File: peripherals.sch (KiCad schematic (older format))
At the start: 23 parts, among them J3 CTC Header, J5 Port B, J6 Port A, J7 PIO Header, U4 CTC - Z84C3010AEG, U5 SIO/3 - Z84C4310AEG, U7 Z84C2010AEG

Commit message: reset annotations, added dip switch
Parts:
- renumbered J3 to J6, J5 to J7, J6 to J8, J7 to J9, R27 to R36, R28 to R37, R29 to R38, R30 to R39, R31 to R40, R32 to R41, R33 to R42, R34 to R43, R35 to R44, R36 to R45, R37 to R46, R38 to R47, R39 to R48, R40 to R49, R41 to R50, R42 to R51, U4 to U7, U5 to U8, U7 to U9

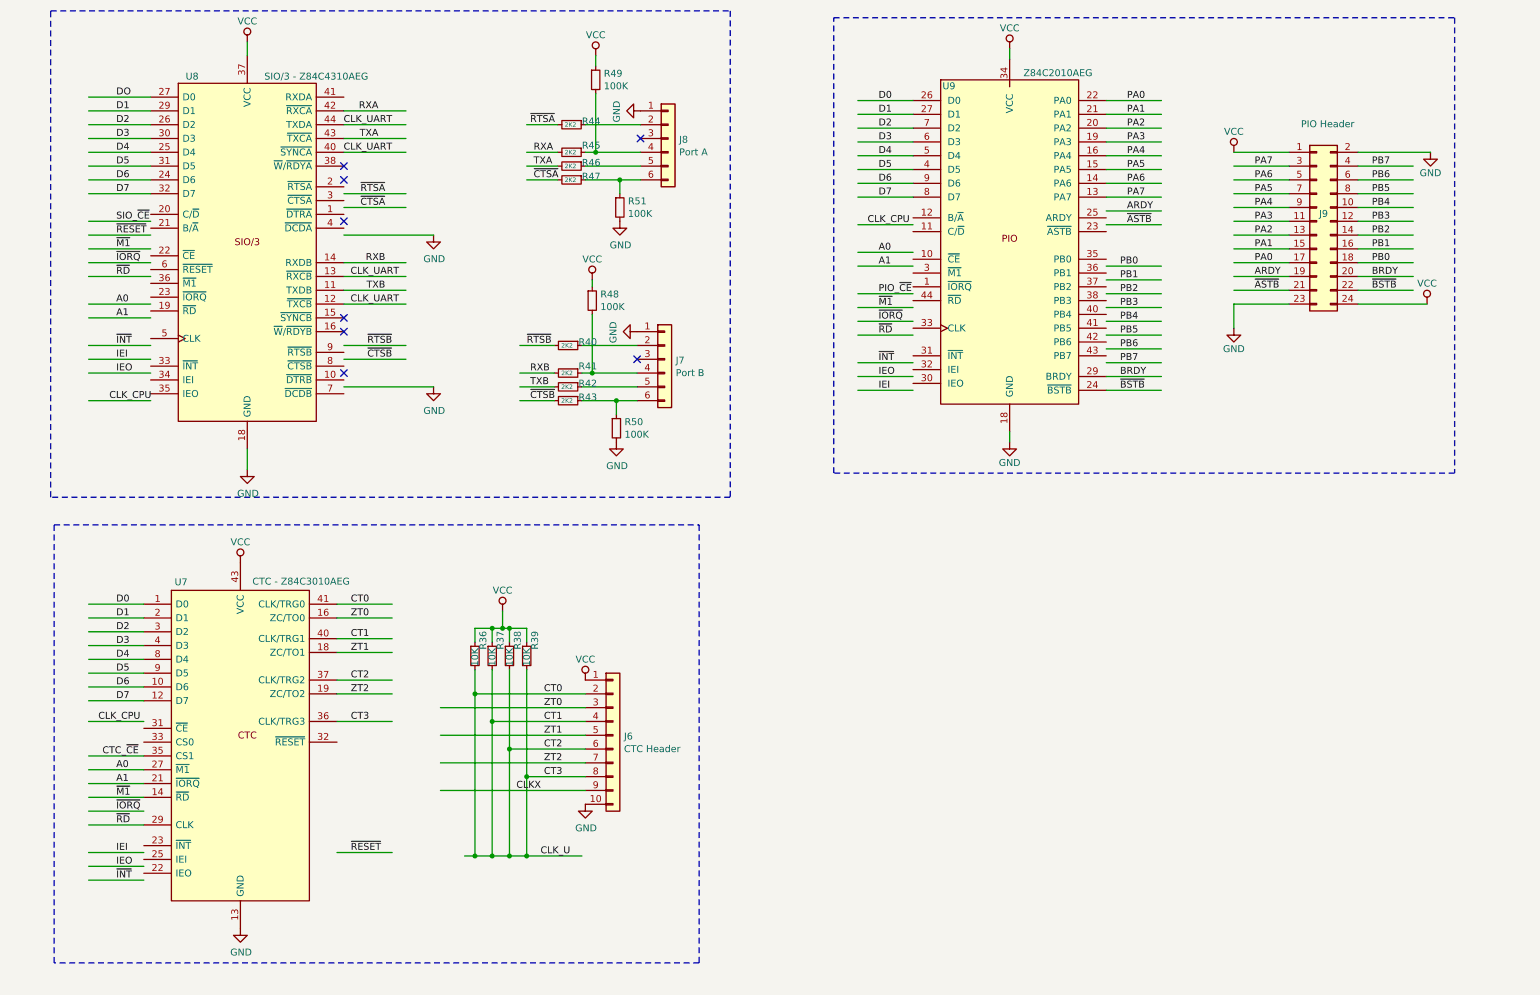
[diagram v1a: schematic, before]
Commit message: connect sheet pins
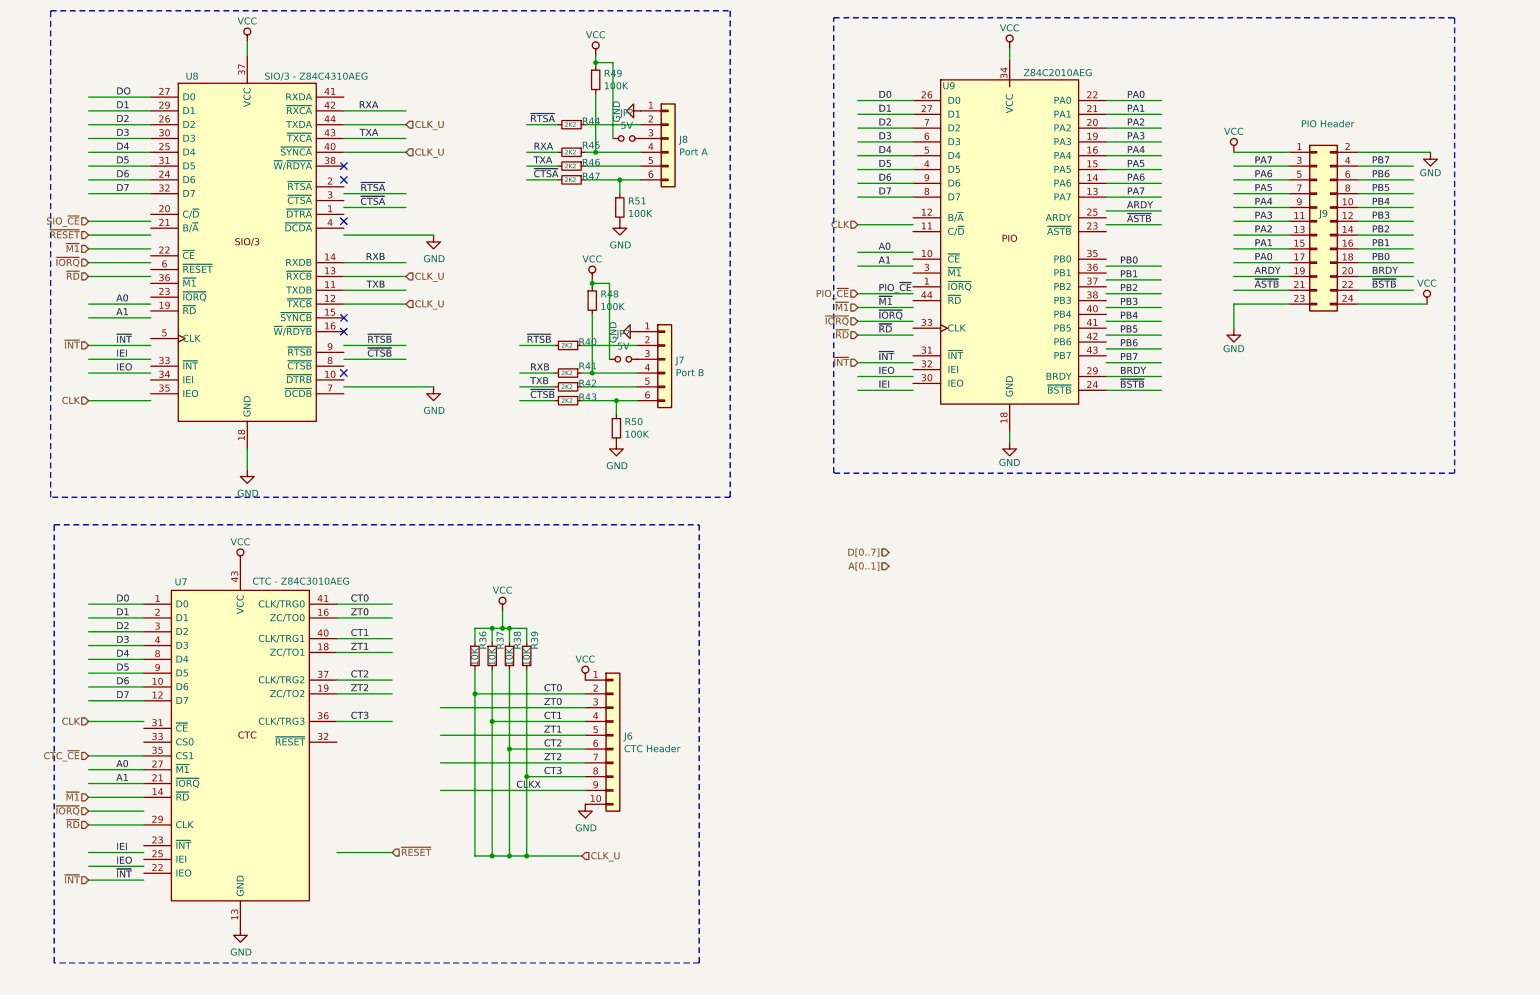
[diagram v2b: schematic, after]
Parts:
- added JP? (x2): 5V, Connector_PinHeader_2.54mm:PinHeader_1x02_P2.54mm_Vertical, symbol Device:Jumper_NO_Small
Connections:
- net labels added: A[0..1], CLK, CTC_~CE, D[0..7], PIO_~CE, SIO_~CE
- net labels removed: CLK_CPU, CLK_UART, CTC_~CE~, SIO_~CE~
- wire segments 182 -> 187
- no-connect marks 8 -> 6
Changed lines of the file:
@@
 $Descr A4 11693 8268
 encoding utf-8
-Sheet 3 3
+Sheet 2 3
 Title ""
 Date ""
@@
 Text Label 6625 1950 0    50   ~ 0
 D7
-Text Label 6850 2150 2    50   ~ 0
-CLK_CPU
 Text Label 6625 2350 0    50   ~ 0
 A0
@@
 Text Label 4100 3225 0    50   ~ 0
 RXB
-Text Label 3150 2725 2    50   ~ 0
-CLK_UART
-Text Label 3150 2525 2    50   ~ 0
-CLK_UART
-Text Label 1100 2125 0    50   ~ 0
-SIO_~CE~
-Text Label 3100 1625 2    50   ~ 0
-CLK_UART
-Text Label 3100 1425 2    50   ~ 0
-CLK_UART
 Text Label 3100 3025 2    50   ~ 0
 ~RTSB
@@
 	1    0    0    -1
 $EndComp
-Text Label 1050 3425 0    50   ~ 0
-CLK_CPU
 Text Label 1100 3225 0    50   ~ 0
 IEO
@@
 Text Label 1100 2725 0    50   ~ 0
 A0
-Text Label 1100 2525 0    50   ~ 0
-~RD
-Text Label 1100 2325 0    50   ~ 0
-~M1
 $Comp
 L THS-80:Z84C4310AEG U?
@@
 	1    0    0    -1
 $EndComp
-Text Label 1100 2225 0    50   ~ 0
-~RESET
-Text Label 1100 2425 0    50   ~ 0
-~IORQ
-Wire Wire Line
-	4575 925  4575 1000
-Wire Wire Line
-	4550 2550 4550 2600
+Wire Wire Line
+	4575 925  4575 975
+Wire Wire Line
+	4550 2550 4550 2575
 Wire Wire Line
 	4275 3425 4025 3425
@@
 Wire Wire Line
 	4900 1425 4500 1425
-NoConn ~ 4900 1525
 Connection ~ 4725 3425
 Connection ~ 4550 3225
-NoConn ~ 4875 3125
 Connection ~ 4750 1825
 Connection ~ 4575 1625
@@
 Wire Wire Line
 	1300 6900 900  6900
-Text Label 1275 5750 2    50   ~ 0
-CLK_CPU
-Text Label 1000 6000 0    50   ~ 0
-CTC_~CE~
 Text Label 1100 6800 0    50   ~ 0
 IEO
@@
 Text Label 1100 6700 0    50   ~ 0
 IEI
-Text Label 1100 6300 0    50   ~ 0
-~M1
-Text Label 1100 6400 0    50   ~ 0
-~IORQ
-Text Label 1100 6500 0    50   ~ 0
-~RD
 Text Label 1100 6100 0    50   ~ 0
 A0
@@
 Text Label 2800 5750 0    50   ~ 0
 CT3
-Text Label 2800 6700 0    50   ~ 0
-~RESET
 Wire Wire Line
 	3450 5650 4500 5650
@@
 Wire Wire Line
 	3450 6250 4500 6250
-Wire Wire Line
-	3625 6725 3700 6725
 Wire Wire Line
 	4075 6150 4075 6725
@@
 	3700 5550 3700 6725
 Connection ~ 3700 5550
-Connection ~ 3700 6725
 Wire Wire Line
 	3700 6725 3825 6725
-Text Label 4175 6725 0    50   ~ 0
-CLK_U
 Wire Notes Line
 	650  4325 5325 4325
@@
 Wire Wire Line
 	9200 2725 9200 2900
+Text HLabel 6700 4525 0    50   Input ~ 0
+D[0..7]
+Text HLabel 6700 4625 0    50   Input ~ 0
+A[0..1]
+Text HLabel 3100 6700 2    50   Input ~ 0
+~RESET
+Text HLabel 900  5750 0    50   Input ~ 0
+CLK
+Text HLabel 900  6000 0    50   Input ~ 0
+CTC_~CE
+Text HLabel 900  6300 0    50   Input ~ 0
+~M1
+Text HLabel 900  6400 0    50   Input ~ 0
+~IORQ
+Text HLabel 900  6500 0    50   Input ~ 0
+~RD
+Text HLabel 900  2225 0    50   Input ~ 0
+~RESET
+Text HLabel 900  2125 0    50   Input ~ 0
+SIO_~CE
+Text HLabel 900  2325 0    50   Input ~ 0
+~M1
+Text HLabel 900  2425 0    50   Input ~ 0
+~IORQ
+Text HLabel 900  2525 0    50   Input ~ 0
+~RD
+Text HLabel 900  3425 0    50   Input ~ 0
+CLK
+Text HLabel 6475 2150 0    50   Input ~ 0
+CLK
+Text HLabel 6475 2750 0    50   Input ~ 0
+~M1
+Text HLabel 6475 2850 0    50   Input ~ 0
+~IORQ
+Text HLabel 6475 2950 0    50   Input ~ 0
+~RD
+Text HLabel 6475 2650 0    50   Input ~ 0
+PIO_~CE
+Text HLabel 900  3025 0    50   Input ~ 0
+~INT
+Text HLabel 900  6900 0    50   Input ~ 0
+~INT
+Text HLabel 6475 3150 0    50   Input ~ 0
+~INT
+Text HLabel 4475 6725 2    50   Input ~ 0
+CLK_U
+$Comp
+L Device:Jumper_NO_Small JP?
+U 1 1 5D92266C
+P 4775 3125
+F 0 "JP?" H 4775 3310 50  0000 C CNN
+F 1 "5V" H 4775 3219 50  0000 C CNN
+F 2 "Connector_PinHeader_2.54mm:PinHeader_1x02_P2.54mm_Vertical" H 4775 3125 50  0001 C CNN
+F 3 "~" H 4775 3125 50  0001 C CNN
+	1    4775 3125
+	1    0    0    -1
+$EndComp
+Wire Wire Line
+	4675 3125 4675 2575
+Wire Wire Line
+	4675 2575 4550 2575
+Connection ~ 4550 2575
+Wire Wire Line
+	4550 2575 4550 2600
+$Comp
+L Device:Jumper_NO_Small JP?
+U 1 1 5D934FDF
+P 4800 1525
+F 0 "JP?" H 4800 1710 50  0000 C CNN
+F 1 "5V" H 4800 1619 50  0000 C CNN
+F 2 "Connector_PinHeader_2.54mm:PinHeader_1x02_P2.54mm_Vertical" H 4800 1525 50  0001 C CNN
+F 3 "~" H 4800 1525 50  0001 C CNN
+	1    4800 1525
+	1    0    0    -1
+$EndComp
+Wire Wire Line
+	4700 1525 4700 975
+Wire Wire Line
+	4700 975  4575 975
+Connection ~ 4575 975
+Wire Wire Line
+	4575 975  4575 1000
+Text HLabel 3200 2725 2    50   Input ~ 0
+CLK_U
+Text HLabel 3200 2525 2    50   Input ~ 0
+CLK_U
+Text HLabel 3200 1625 2    50   Input ~ 0
+CLK_U
+Text HLabel 3200 1425 2    50   Input ~ 0
+CLK_U
 $EndSCHEMATC

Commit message: connected sheet pins to bus
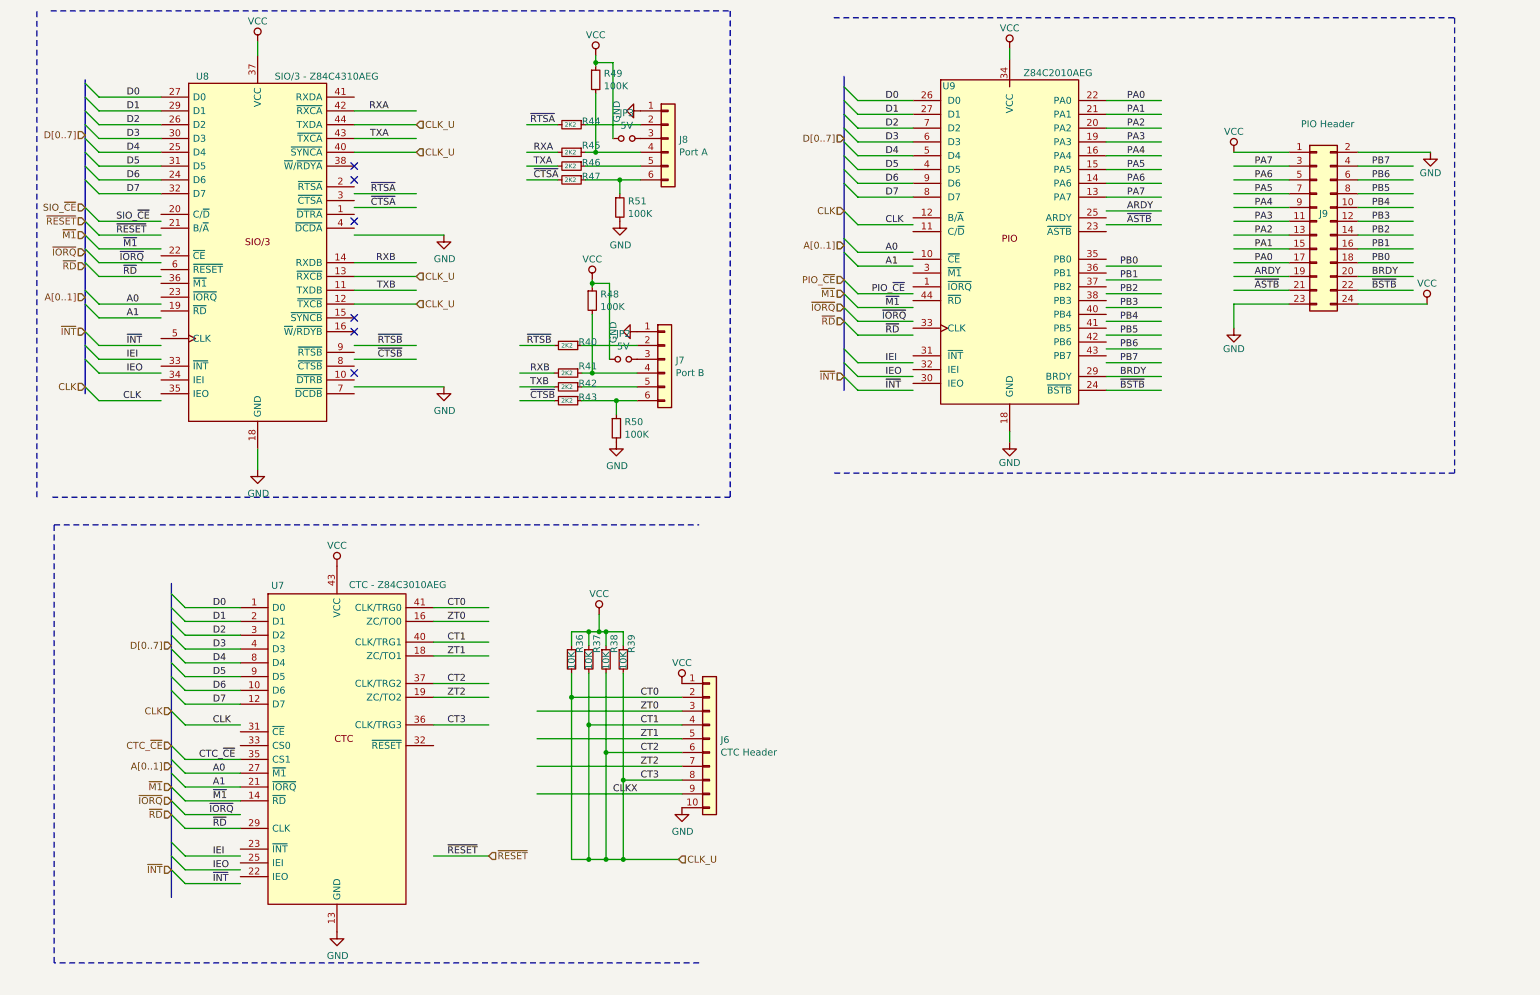
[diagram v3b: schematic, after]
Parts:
- gave numbers to parts that had none: 2
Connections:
- net labels removed: DO, PIO_~CE~
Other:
- moved on the sheet: J6, R36, R37, R38, R39, U7, U8

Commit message: Moved CPU, RAM, ROM to sub-sheet
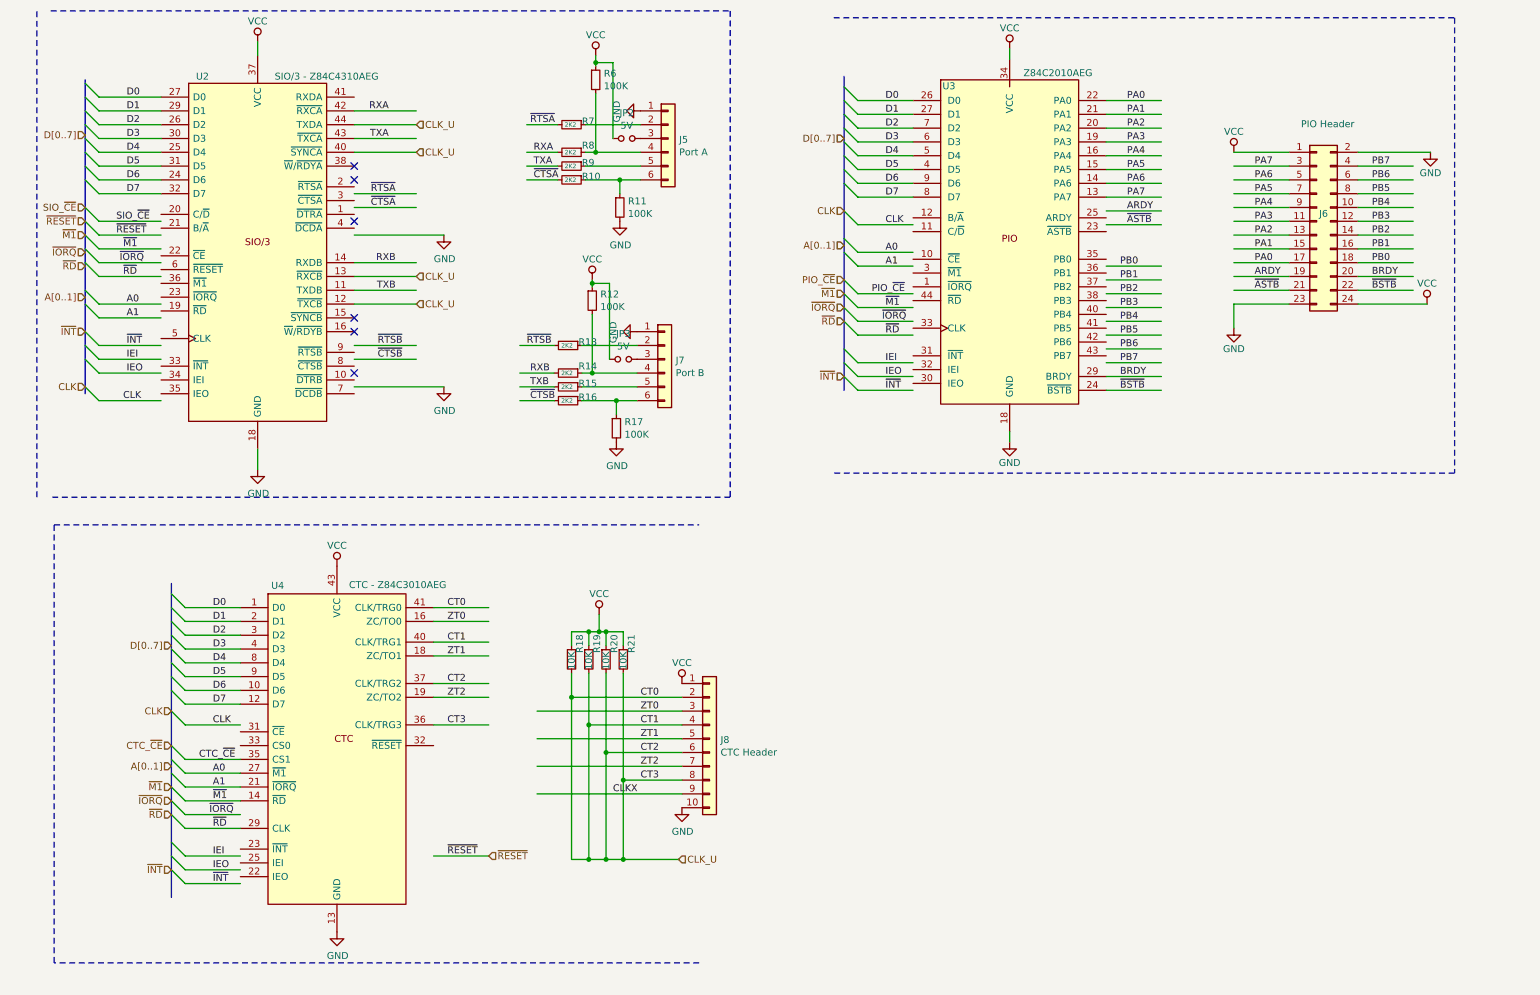
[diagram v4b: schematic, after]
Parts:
- renumbered J8 to J5, J9 to J6, J6 to J8, JP3 to JP2, JP2 to JP3, R47 to R10, R51 to R11, R48 to R12, R40 to R13, R41 to R14, R42 to R15, R43 to R16, R50 to R17, R36 to R18, R37 to R19, R38 to R20, R39 to R21, R49 to R6, R44 to R7, R45 to R8, R46 to R9, U8 to U2, U9 to U3, U7 to U4

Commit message: fixed up interrupt chain wiring
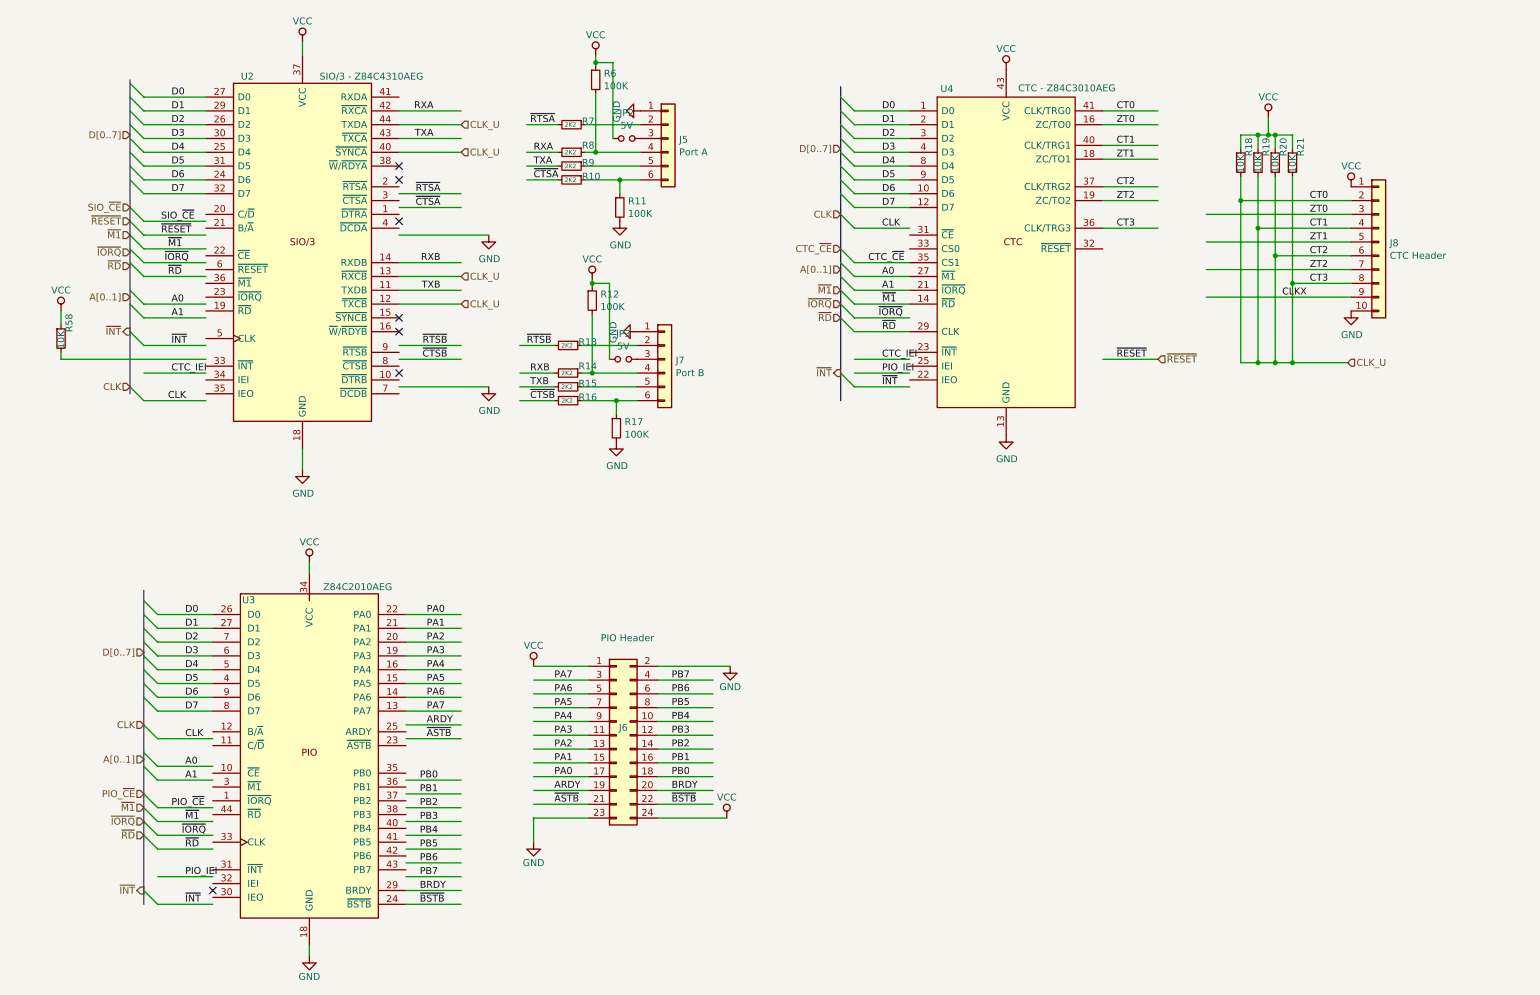
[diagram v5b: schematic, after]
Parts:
- added R58: 10K, Resistor_SMD:R_0603_1608Metric_Pad1.05x0.95mm_HandSolder, symbol THS-80-rescue:R_Small-Device-sbc_z80-rescue
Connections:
- net labels added: CTC_IEI, PIO_IEI
- net labels removed: IEI, IEO
- wire segments 187 -> 188
- no-connect marks 6 -> 7
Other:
- moved on the sheet: J6, J8, R18, R19, R20, R21, U2, U3, U4

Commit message: passed DRC
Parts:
- removed R58: 10K, Resistor_SMD:R_0603_1608Metric_Pad1.05x0.95mm_HandSolder, symbol THS-80-rescue:R_Small-Device-sbc_z80-rescue
- removed U2: SIO/3 - Z84C4310AEG, Package_QFP:LQFP-44_10x10mm_P0.8mm, symbol THS-80:Z84C4310AEG
- removed U3: Z84C2010AEG, Package_QFP:LQFP-44_10x10mm_P0.8mm, symbol THS-80:Z84C2010AEG
- removed U4: CTC - Z84C3010AEG, Package_QFP:LQFP-44_10x10mm_P0.8mm, symbol THS-80:Z84C3010AEG
- added C19, C20, C21: 100nF, Capacitor_SMD:C_0603_1608Metric_Pad1.05x0.95mm_HandSolder, symbol Device:C_Small
- added R22: 10K, Resistor_SMD:R_0603_1608Metric_Pad1.05x0.95mm_HandSolder, symbol Device:R_Small
- added U7: Z84C2010AEG, Package_QFP:LQFP-44_10x10mm_P0.8mm, symbol THS-80:Z84C2010AEG
- added U8: Z84C4310AEG, Package_QFP:LQFP-44_10x10mm_P0.8mm, symbol THS-80:Z84C4310AEG
- added U9: Z84C3010AEG, Package_QFP:LQFP-44_10x10mm_P0.8mm, symbol THS-80:Z84C3010AEG
- renumbered J8 to J10, J6 to J7, J7 to J8, J5 to J9, JP3 to JP2, JP2 to JP3, R13 to R23, R14 to R24, R15 to R25, R16 to R26, R7 to R27, R8 to R28, R9 to R29, R10 to R30, R12 to R31, R6 to R32, R17 to R33, R11 to R34, R18 to R35, R19 to R36, R20 to R37, R21 to R38
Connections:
- net labels added: CLK_A, CLK_B, CLK_C, IEI, IEO, IEO_0, IEO_1, PIO_~CE~, SIO_~CE~, ~RESET~
- net labels removed: CLKX, CTC_IEI, PIO_IEI, PIO_~CE, SIO_~CE, ZT0, ZT1, ZT2, ~RESET
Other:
- moved on the sheet: J10, J7, J8, J9, JP2, JP3, R23, R24, R25, R26, R27, R28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
